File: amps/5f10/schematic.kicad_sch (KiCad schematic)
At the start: 42 parts, among them T1 PP OT

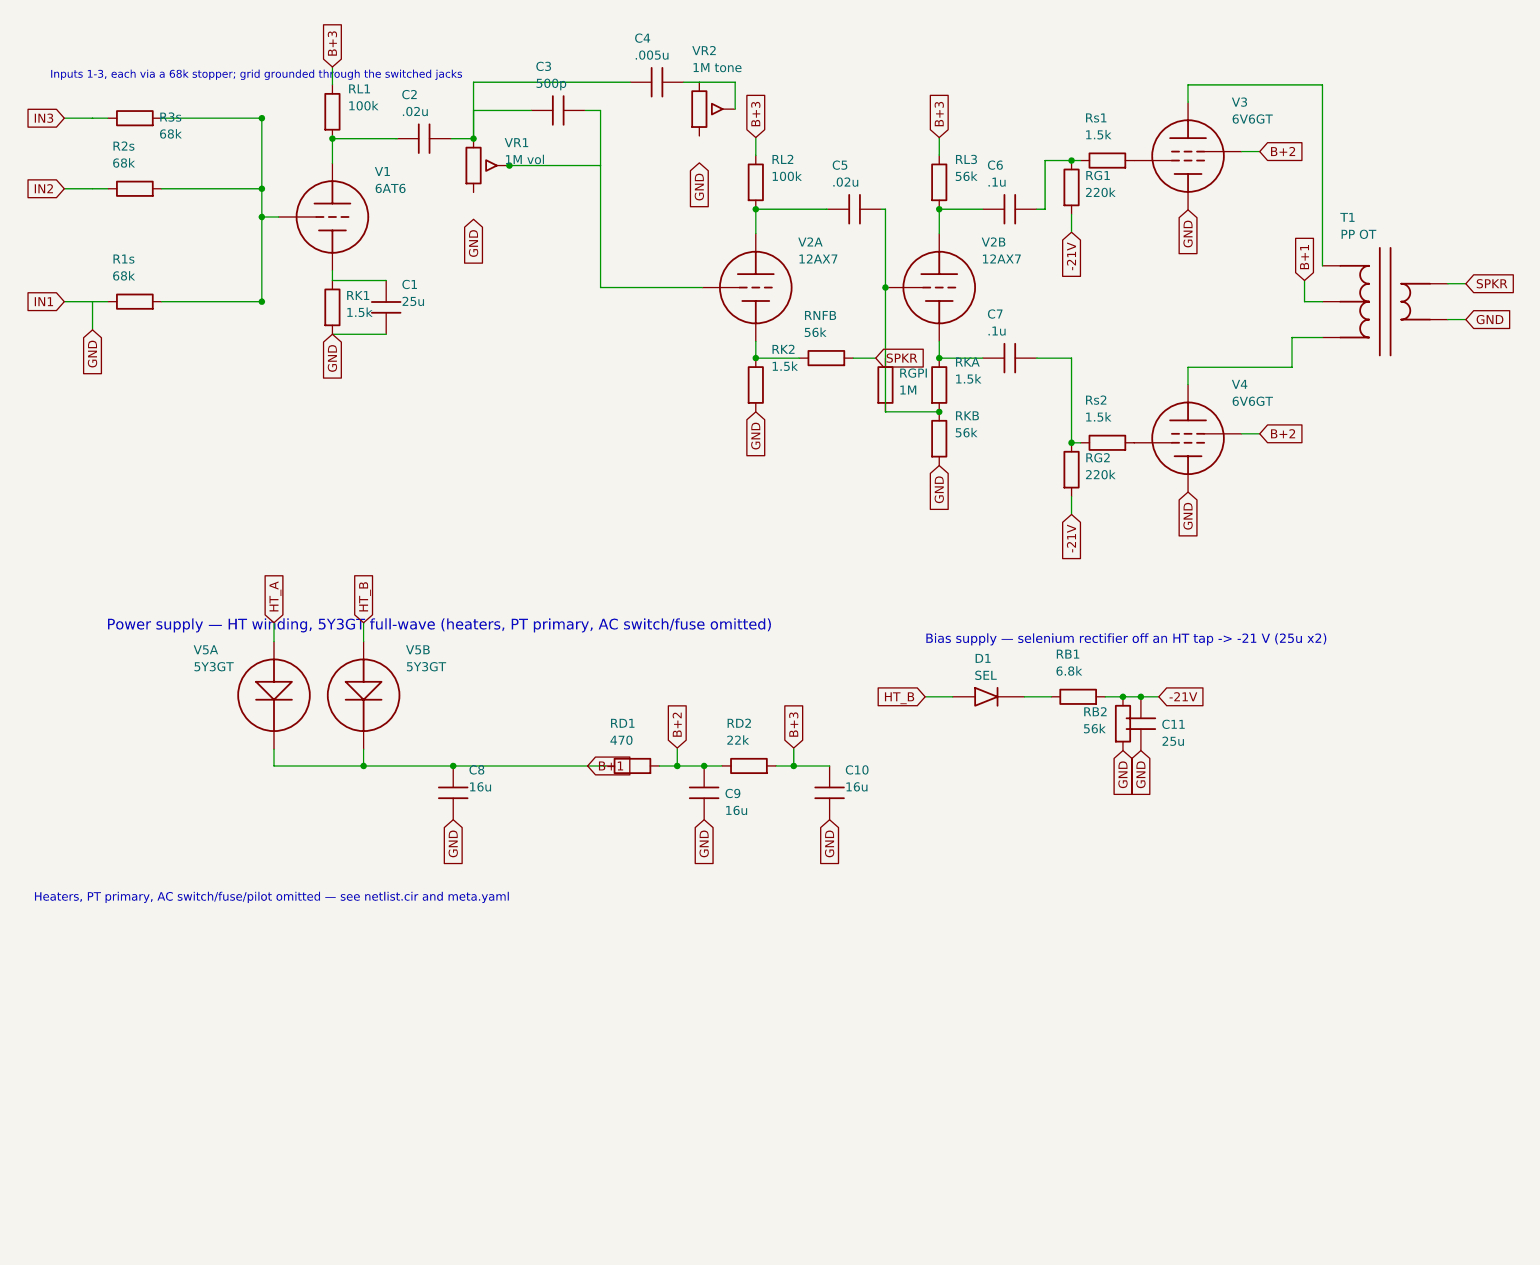
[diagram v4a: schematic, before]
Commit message: Fix: deterministic schematic ids and wires split at every join
- _u() is uuid5 over (amp id, emission order), so a regeneration of an
  unchanged script is byte-identical and a drift gate becomes possible
- write() splits wire segments at symbol pins, wire ends and junction dots,
  so the file connects exactly what the drawing shows under KiCad's
  endpoint-only semantics (270 pins were on a wire's interior; net
  partitions unchanged on all 38 sheets)
- all sheets regenerated; aa864-bassman title block was stale (draft) and
  now matches meta.yaml (verified)

Co-Authored-By: Claude Fable 5.1 <noreply@anthropic.com>
Claude-Session: https://claude.ai/code/session_01KBMfdh37HmCL2iWcBiL5J1
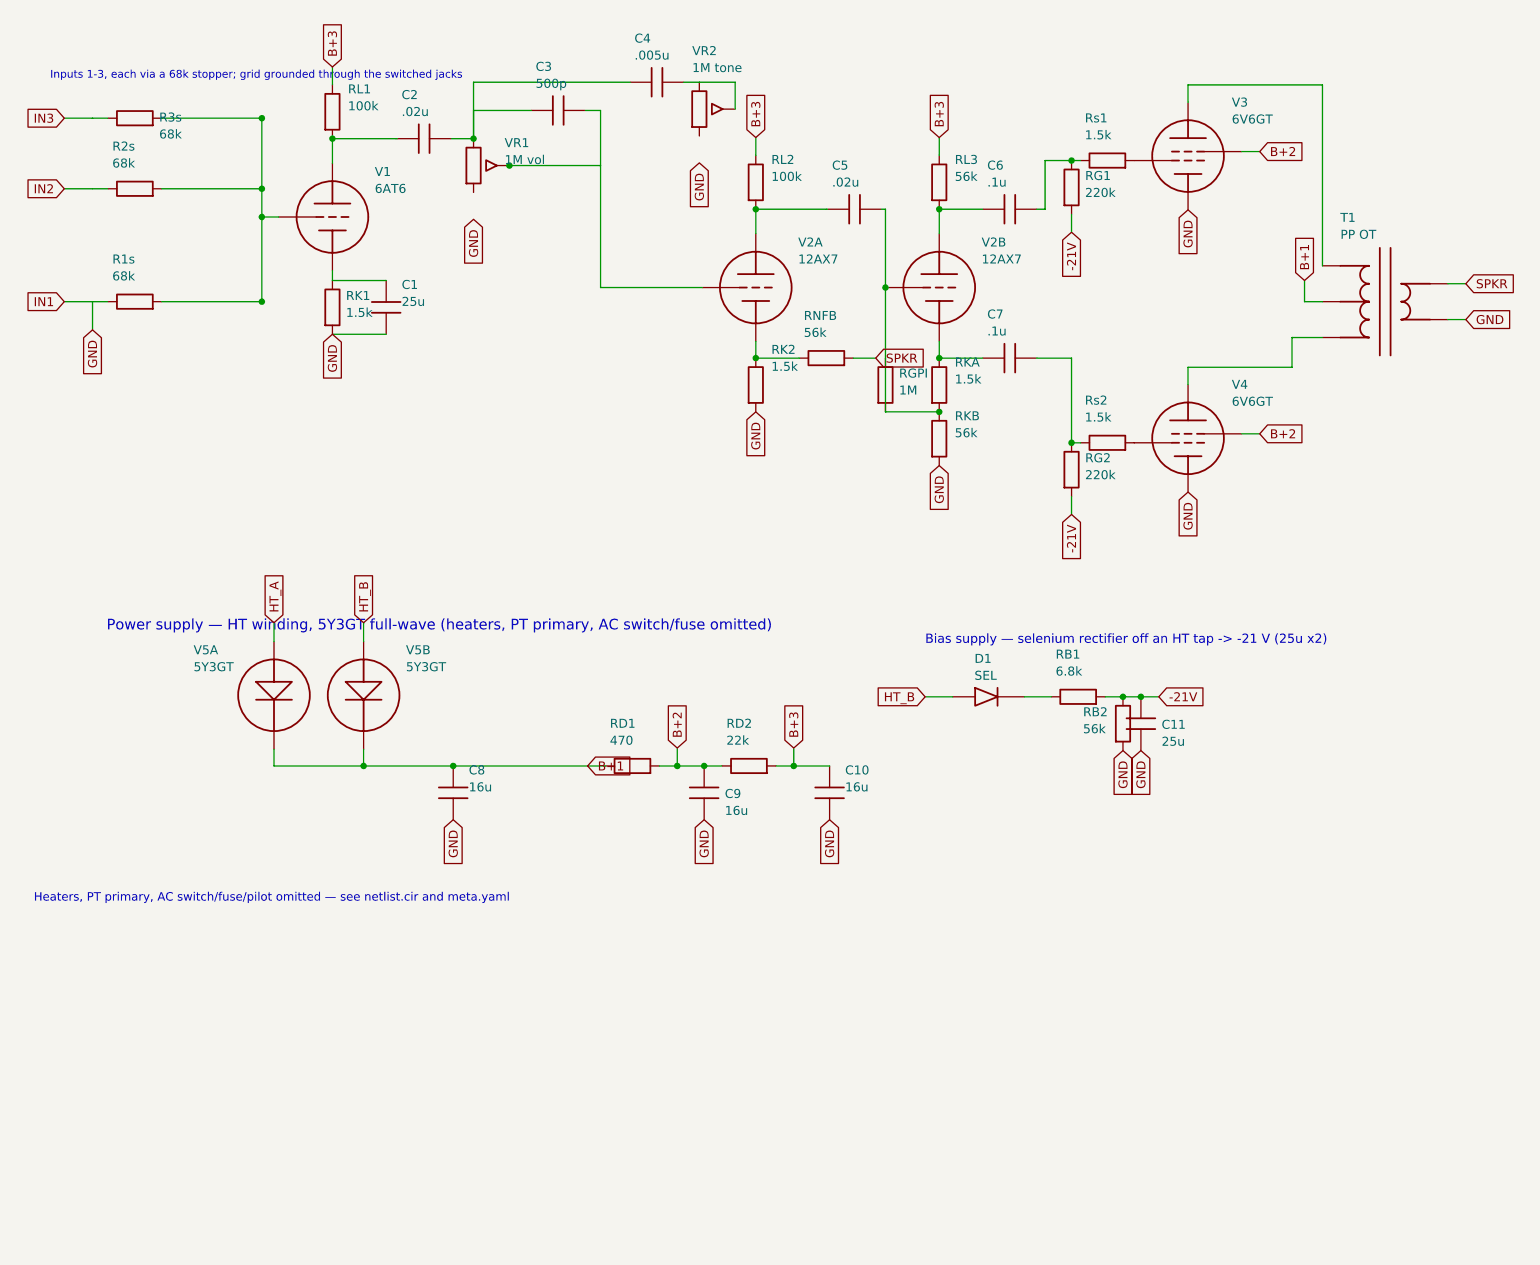
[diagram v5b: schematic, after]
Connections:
- net at C5.2, RGPI.2, RKA.2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: now also RGPI.1
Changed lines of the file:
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@@
   (wire (pts (xy 21.018 50.889) (xy 21.018 54.889))
     (stroke (width 0) (type default)))
-  (wire (pts (xy 45.018 24.889) (xy 45.018 50.889))
+  (wire (pts (xy 45.018 24.889) (xy 45.018 34.889))
+    (stroke (width 0) (type default)))
+  (wire (pts (xy 45.018 34.889) (xy 45.018 38.889))
+    (stroke (width 0) (type default)))
+  (wire (pts (xy 45.018 38.889) (xy 45.018 50.889))
     (stroke (width 0) (type default)))
   (text "Inputs 1-3, each via a 68k stopper; grid grounded through the switched jacks" (at 15.018 18.889 0)
@@
     (stroke (width 0) (type default)))
   (junction (at 80.098 31.599) (diameter 0) (color 0 0 0 0))
-  (wire (pts (xy 75.018 27.789) (xy 75.018 19.789))
+  (wire (pts (xy 75.018 27.789) (xy 75.018 23.789))
+    (stroke (width 0) (type default)))
+  (wire (pts (xy 75.018 23.789) (xy 75.018 19.789))
     (stroke (width 0) (type default)))
   (junction (at 75.018 27.789) (diameter 0) (color 0 0 0 0))
@@
   (global_label "GND" (shape input) (at 141.018 74.119 270)
     (effects (font (size 1.27 1.27)) (justify right)))
-  (wire (pts (xy 133.398 48.889) (xy 133.398 66.509))
+  (wire (pts (xy 133.398 48.889) (xy 133.398 58.889))
+    (stroke (width 0) (type default)))
+  (wire (pts (xy 133.398 58.889) (xy 133.398 66.509))
     (stroke (width 0) (type default)))
   (junction (at 133.398 48.889) (diameter 0) (color 0 0 0 0))
@@
   (wire (pts (xy 59.438 114.289) (xy 59.438 116.689))
     (stroke (width 0) (type default)))
-  (wire (pts (xy 46.738 116.689) (xy 91.188 116.689))
+  (wire (pts (xy 46.738 116.689) (xy 59.438 116.689))
+    (stroke (width 0) (type default)))
+  (wire (pts (xy 59.438 116.689) (xy 72.138 116.689))
+    (stroke (width 0) (type default)))
+  (wire (pts (xy 72.138 116.689) (xy 91.188 116.689))
     (stroke (width 0) (type default)))
   (junction (at 59.438 116.689) (diameter 0) (color 0 0 0 0))
@@
     (property "Reference" "RD1" (at 94.338 110.689 270) (effects (font (size 1.27 1.27)) (justify left)))
     (property "Value" "470" (at 94.338 113.089 270) (effects (font (size 1.27 1.27)) (justify left))))
-  (wire (pts (xy 101.348 116.689) (xy 110.238 116.689))
+  (wire (pts (xy 101.348 116.689) (xy 103.888 116.689))
+    (stroke (width 0) (type default)))
+  (wire (pts (xy 103.888 116.689) (xy 107.698 116.689))
+    (stroke (width 0) (type default)))
+  (wire (pts (xy 107.698 116.689) (xy 110.238 116.689))
     (stroke (width 0) (type default)))
   (junction (at 103.888 116.689) (diameter 0) (color 0 0 0 0))
@@
     (property "Reference" "RD2" (at 110.848 110.689 270) (effects (font (size 1.27 1.27)) (justify left)))
     (property "Value" "22k" (at 110.848 113.089 270) (effects (font (size 1.27 1.27)) (justify left))))
-  (wire (pts (xy 117.858 116.689) (xy 125.478 116.689))
+  (wire (pts (xy 117.858 116.689) (xy 120.398 116.689))
+    (stroke (width 0) (type default)))
+  (wire (pts (xy 120.398 116.689) (xy 125.478 116.689))
     (stroke (width 0) (type default)))
   (junction (at 120.398 116.689) (diameter 0) (color 0 0 0 0))
@@
   (wire (pts (xy 156.898 106.889) (xy 156.898 106.889))
     (stroke (width 0) (type default)))
-  (wire (pts (xy 164.518 106.889) (xy 172.138 106.889))
+  (wire (pts (xy 164.518 106.889) (xy 167.058 106.889))
+    (stroke (width 0) (type default)))
+  (wire (pts (xy 167.058 106.889) (xy 169.598 106.889))
+    (stroke (width 0) (type default)))
+  (wire (pts (xy 169.598 106.889) (xy 172.138 106.889))
     (stroke (width 0) (type default)))
   (junction (at 167.058 106.889) (diameter 0) (color 0 0 0 0))

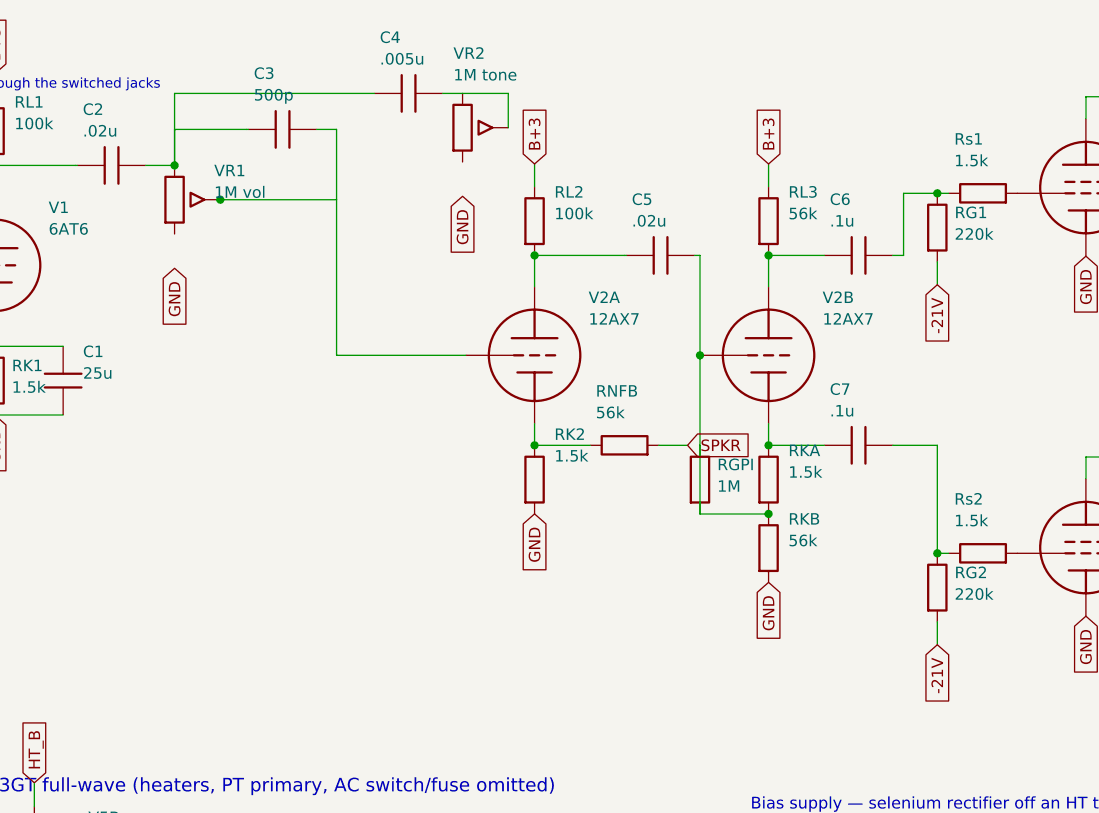
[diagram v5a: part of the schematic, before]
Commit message: Fix: schematic wiring on the tweed family, jtm45 and 6161
- pot cold lugs: s.gnd() sat 3.81 mm below cx:POT pin 3 on nine sheets
  (19 pins); every flag now lands on the lug
- retyped coordinates replaced by helper returns (5e5a OT pins alone freed
  nine pins; 5d3 V3 cathode, 5f10 RKB, 5e6a CBS, 5f2a dropper, grid leaks)
- shorts only verify_schematic_nets could see: 5e3 cathode bus through V4's
  screen pin (B+2 tied to the cathodes), C7 through RG6A, PI leak through
  RGPI, C8 on the cathode not the tail; 5f10 the same RGPI/C7 pair; 5e5a
  presence feed down the tube column; 5e6a RFB loop through RL3
- three dated waivers: two-terminal rheostat far lugs (5e6a VR5, 6161 VR3/VR4)

Co-Authored-By: Claude Fable 5.1 <noreply@anthropic.com>
Claude-Session: https://claude.ai/code/session_01KBMfdh37HmCL2iWcBiL5J1
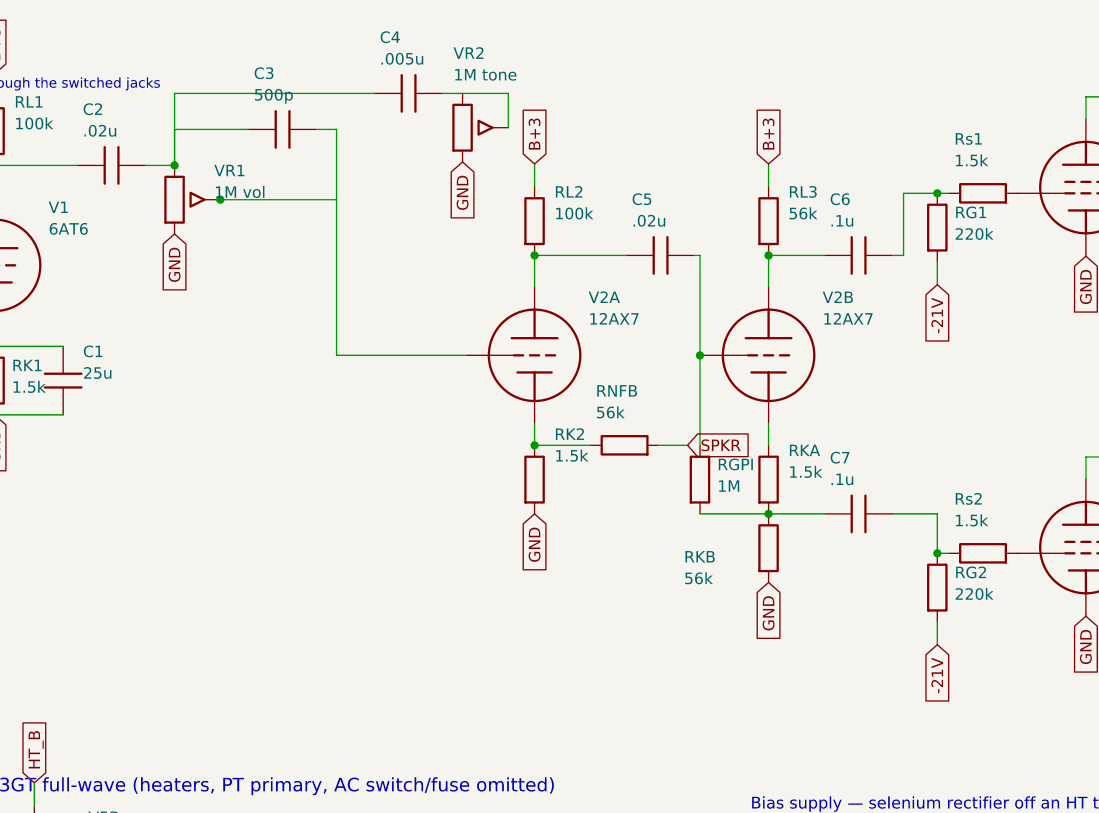
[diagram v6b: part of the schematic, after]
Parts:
- removed RB1: 6.8k, symbol cx:R
- removed RD2: 22k, symbol cx:R
- removed V3, V4: 6V6GT, symbol cx:PENTODE
- added C9: 16u, symbol cx:C
- added D1: SEL, symbol cx:DIODE_SS
- added Rs1, Rs2: 1.5k, symbol cx:R
- RB1: renamed from D1; value SEL -> 6.8k; symbol cx:DIODE_SS -> cx:R
- RD2: renamed from C9; value 16u -> 22k; symbol cx:C -> cx:R
- V3: renamed from Rs1; value 1.5k -> 6V6GT; symbol cx:R -> cx:PENTODE
- V4: renamed from Rs2; value 1.5k -> 6V6GT; symbol cx:R -> cx:PENTODE
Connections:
- net -21V: now also RB1.2
- net B+2: now also V3.3 (G2), V4.3 (G2), C9.1
- net B+3: now also RD2.2
- net GND: now also V3.4 (K), V4.4 (K), VR1.3, VR2.3, C9.2; no longer RD2.2
- net HT_B: now also D1.1 (A); no longer RB1.1 (A)
- net at RKA.1, V2B.3 (K): no longer C7.1
- net at C5.2, RGPI.1, V2B.2 (G): no longer RGPI.2, RKA.2
- net at C6.2, RG1.1: now also Rs1.1; no longer V3.1
- net at V3.2 (G1): now also Rs1.2
- net at RKB.1: now also C7.1, RGPI.2, RKA.2
- net at T1.1 (PRI_A): now also V3.1 (P)
- net at C7.2, RG2.1: now also Rs2.1; no longer V4.1
- net at T1.3 (PRI_B): now also V4.1 (P)
- net at V4.2 (G1): now also Rs2.2
- new net: D1.2 (K), RB1.1
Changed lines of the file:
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@@
     (property "Reference" "VR1" (at 79.418 28.399 0) (effects (font (size 1.27 1.27)) (justify left)))
     (property "Value" "1M vol" (at 79.418 30.799 0) (effects (font (size 1.27 1.27)) (justify left))))
-  (global_label "GND" (shape input) (at 75.018 39.219 270)
+  (global_label "GND" (shape input) (at 75.018 35.409 270)
     (effects (font (size 1.27 1.27)) (justify right)))
   (wire (pts (xy 75.018 27.789) (xy 75.018 23.789))
@@
     (property "Reference" "VR2" (at 106.002 15.359 0) (effects (font (size 1.27 1.27)) (justify left)))
     (property "Value" "1M tone" (at 106.002 17.759 0) (effects (font (size 1.27 1.27)) (justify left))))
-  (global_label "GND" (shape input) (at 107.018 31.219 270)
+  (global_label "GND" (shape input) (at 107.018 27.409 270)
     (effects (font (size 1.27 1.27)) (justify right)))
   (wire (pts (xy 112.098 23.599) (xy 112.098 19.789))
@@
     (property "Value" "1.5k" (at 143.218 61.899 0) (effects (font (size 1.27 1.27)) (justify left))))
   (junction (at 141.018 66.509) (diameter 0) (color 0 0 0 0))
-  (symbol (lib_id "cx:R") (at 141.018 70.309 0) (unit 1)
+  (symbol (lib_id "cx:R") (at 141.018 70.319 0) (unit 1)
     (in_bom yes) (on_board yes)
-    (property "Reference" "RKB" (at 143.218 67.109 0) (effects (font (size 1.27 1.27)) (justify left)))
-    (property "Value" "56k" (at 143.218 69.509 0) (effects (font (size 1.27 1.27)) (justify left))))
-  (global_label "GND" (shape input) (at 141.018 74.119 270)
+    (property "Reference" "RKB" (at 131.618 71.319 0) (effects (font (size 1.27 1.27)) (justify left)))
+    (property "Value" "56k" (at 131.618 73.719 0) (effects (font (size 1.27 1.27)) (justify left))))
+  (global_label "GND" (shape input) (at 141.018 74.129 270)
     (effects (font (size 1.27 1.27)) (justify right)))
   (wire (pts (xy 133.398 48.889) (xy 133.398 58.889))
-    (stroke (width 0) (type default)))
-  (wire (pts (xy 133.398 58.889) (xy 133.398 66.509))
     (stroke (width 0) (type default)))
   (junction (at 133.398 48.889) (diameter 0) (color 0 0 0 0))
@@
   (wire (pts (xy 156.018 30.889) (xy 159.768 30.889))
     (stroke (width 0) (type default)))
-  (wire (pts (xy 141.018 58.889) (xy 147.208 58.889))
+  (wire (pts (xy 141.018 66.509) (xy 147.208 66.509))
     (stroke (width 0) (type default)))
-  (junction (at 141.018 58.889) (diameter 0) (color 0 0 0 0))
-  (symbol (lib_id "cx:C") (at 151.018 58.889 90) (unit 1)
+  (symbol (lib_id "cx:C") (at 151.018 66.509 90) (unit 1)
     (in_bom yes) (on_board yes)
-    (property "Reference" "C7" (at 147.818 52.689 270) (effects (font (size 1.27 1.27)) (justify left)))
-    (property "Value" ".1u" (at 147.818 55.089 270) (effects (font (size 1.27 1.27)) (justify left))))
-  (wire (pts (xy 154.828 58.889) (xy 159.768 58.889))
+    (property "Reference" "C7" (at 147.818 60.309 270) (effects (font (size 1.27 1.27)) (justify left)))
+    (property "Value" ".1u" (at 147.818 62.709 270) (effects (font (size 1.27 1.27)) (justify left))))
+  (wire (pts (xy 154.828 66.509) (xy 159.768 66.509))
     (stroke (width 0) (type default)))
-  (wire (pts (xy 159.768 58.889) (xy 159.768 70.889))
+  (wire (pts (xy 159.768 66.509) (xy 159.768 70.889))
     (stroke (width 0) (type default)))
   (symbol (lib_id "cx:R") (at 164.848 30.889 90) (unit 1)
